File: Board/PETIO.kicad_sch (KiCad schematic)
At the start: 59 parts, among them CN2 PORT_CASSETTE_EDGE, CN3 PORT_IEEE_EDGE, IC11 74138N, IC12 74145N, IC15 VIA, IC17 PIA, IC20 PIA, IC21 7417N, IC22 7400N, IC23 7486N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

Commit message: preview for r1.3
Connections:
- net SCA renamed SDA
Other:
- note added: "1.0B: - fix IEEE488 pull up/down resistor values (again) 1.1A: - fully decode PIA addresses - replace some discrete Rs with RN7 - fix 2N2222 footprint for new BOM part 1.2A: - fix addressing 2nd SID by moving BA7 to IC9 - replace JP8 with a solder jumper (I/O block address) - replace 1N4148 with 1N4448 for lower fwd voltage drop 1.3A: - replace std PET kbd connector with extended / IDC conn"
- note added: "CBM-ULTIPET-V1.3A"
- note added: "CBM-ULTIPET-V1.3A-20250806"
- note removed: "1.0B: - fix IEEE488 pull up/down resistor values (again) 1.1A: - fully decode PIA addresses - replace some discrete Rs with RN7 - fix 2N2222 footprint for new BOM part 1.2A: - fix addressing 2nd SID by moving BA7 to IC9 - replace JP8 with a solder jumper (I/O block address) - replace 1N4148 with 1N4448 for lower fwd voltage drop"
- note removed: "CBM-ULTIPET-V1.2A"
- note removed: "CBM-ULTIPET-V1.2A-20241013"
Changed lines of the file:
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@@
 		)
 	)
-	(text "1.0B: \n- fix IEEE488 pull up/down resistor values (again)\n1.1A:\n- fully decode PIA addresses\n- replace some discrete Rs with RN7\n- fix 2N2222 footprint for new BOM part\n1.2A:\n- fix addressing 2nd SID by moving BA7 to IC9\n- replace JP8 with a solder jumper (I/O block address)\n- replace 1N4148 with 1N4448 for lower fwd voltage drop"
+	(text "1.0B: \n- fix IEEE488 pull up/down resistor values (again)\n1.1A:\n- fully decode PIA addresses\n- replace some discrete Rs with RN7\n- fix 2N2222 footprint for new BOM part\n1.2A:\n- fix addressing 2nd SID by moving BA7 to IC9\n- replace JP8 with a solder jumper (I/O block address)\n- replace 1N4148 with 1N4448 for lower fwd voltage drop\n1.3A:\n- replace std PET kbd connector with extended / IDC conn"
 		(exclude_from_sim no)
-		(at 314.706 351.536 0)
+		(at 278.638 347.472 0)
 		(effects
 			(font
@@
 		)
 	)
-	(text "CBM-ULTIPET-V1.2A"
+	(text "CBM-ULTIPET-V1.3A"
 		(exclude_from_sim no)
 		(at 464.82 340.36 0)
@@
 		)
 	)
-	(text "CBM-ULTIPET-V1.2A-20241013\n"
+	(text "CBM-ULTIPET-V1.3A-20250806\n"
 		(exclude_from_sim no)
 		(at 464.82 363.22 0)
@@
 		)
 	)
-	(global_label "SCA"
+	(global_label "SDA"
 		(shape input)
 		(at 76.2 275.59 180)

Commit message: more layout work on r1.3
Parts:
- IC15, IC17, IC20: footprint Package_DIP:DIP-42_W15.24mm_Socket_LongPads -> Package_DIP:DIP-40_W15.24mm_Socket_LongPads
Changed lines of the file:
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@@
 			)
 		)
-		(property "Footprint" "Package_DIP:DIP-42_W15.24mm_Socket_LongPads"
+		(property "Footprint" "Package_DIP:DIP-40_W15.24mm_Socket_LongPads"
 			(at 292.1 203.2 0)
 			(effects
@@
 			)
 		)
-		(property "Footprint" "Package_DIP:DIP-42_W15.24mm_Socket_LongPads"
+		(property "Footprint" "Package_DIP:DIP-40_W15.24mm_Socket_LongPads"
 			(at 154.94 132.08 0)
 			(effects
@@
 			)
 		)
-		(property "Footprint" "Package_DIP:DIP-42_W15.24mm_Socket_LongPads"
+		(property "Footprint" "Package_DIP:DIP-40_W15.24mm_Socket_LongPads"
 			(at 485.14 312.42 0)
 			(effects
@@
 			)
 		)
-		(property "Footprint" "Package_DIP:DIP-42_W15.24mm_Socket_LongPads"
+		(property "Footprint" "Package_DIP:DIP-40_W15.24mm_Socket_LongPads"
 			(at 497.84 312.42 0)
 			(effects
@@
 			)
 		)
-		(property "Footprint" "Package_DIP:DIP-42_W15.24mm_Socket_LongPads"
+		(property "Footprint" "Package_DIP:DIP-40_W15.24mm_Socket_LongPads"
 			(at 469.9 312.42 0)
 			(effects
@@
 			)
 		)
-		(property "Footprint" "Package_DIP:DIP-42_W15.24mm_Socket_LongPads"
+		(property "Footprint" "Package_DIP:DIP-40_W15.24mm_Socket_LongPads"
 			(at 287.02 116.84 0)
 			(effects

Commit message: add some jumper options, layout work
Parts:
- added JP18, JP22: JP1E, cbm_ultipet_v1:JP1, symbol cbm_ultipet_v1-eagle-import:JP1E
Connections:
- net DEC0: now also JP18.1
- net DEC1: now also JP22.1
- new net /IRQ: JP18.2
- new net /NMI: JP22.2
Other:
- note added: "1.0B: - fix IEEE488 pull up/down resistor values (again) 1.1A: - fully decode PIA addresses - replace some discrete Rs with RN7 - fix 2N2222 footprint for new BOM part 1.2A: - fix addressing 2nd SID by moving BA7 to IC9 - replace JP8 with a solder jumper (I/O block address) - replace 1N4148 with 1N4448 for lower fwd voltage drop 1.3A: - replace std PET kbd connector with extended / IDC conn - add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"
- note added: "CBM-ULTIPET-V1.3A-20250809"
- note added: "For use with two-row IDC keyboard connector"
- note removed: "1.0B: - fix IEEE488 pull up/down resistor values (again) 1.1A: - fully decode PIA addresses - replace some discrete Rs with RN7 - fix 2N2222 footprint for new BOM part 1.2A: - fix addressing 2nd SID by moving BA7 to IC9 - replace JP8 with a solder jumper (I/O block address) - replace 1N4148 with 1N4448 for lower fwd voltage drop 1.3A: - replace std PET kbd connector with extended / IDC conn"
- note removed: "CBM-ULTIPET-V1.3A-20250806"

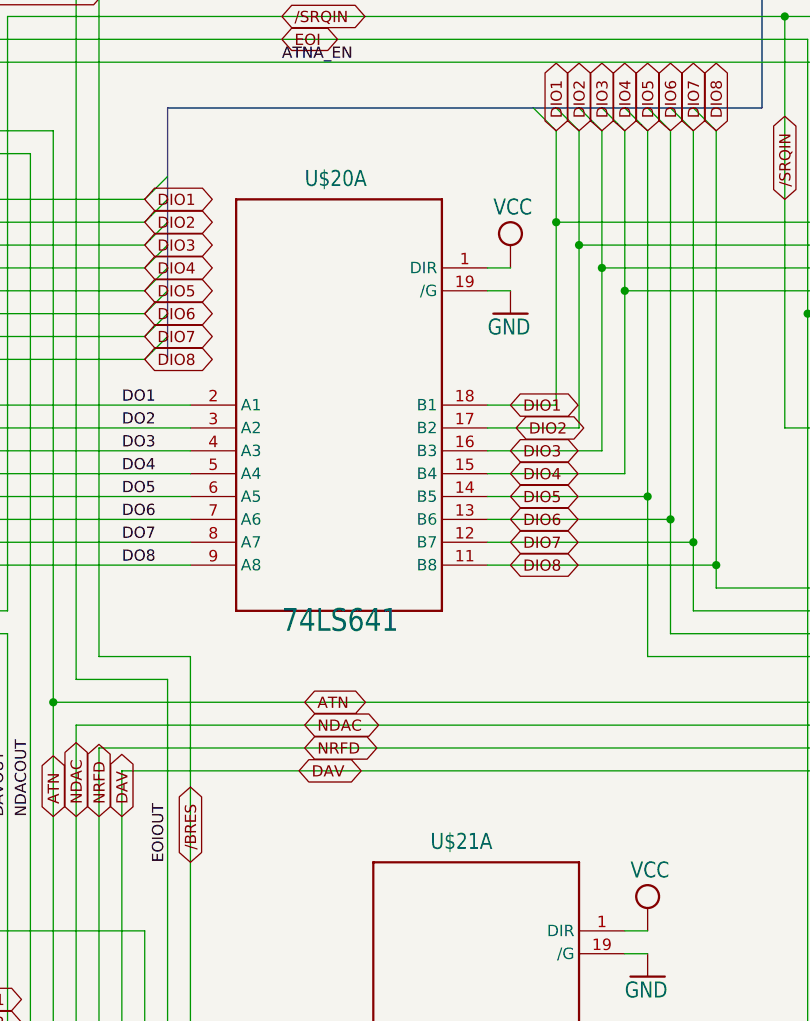
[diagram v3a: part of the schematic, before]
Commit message: rename U refs to UX*
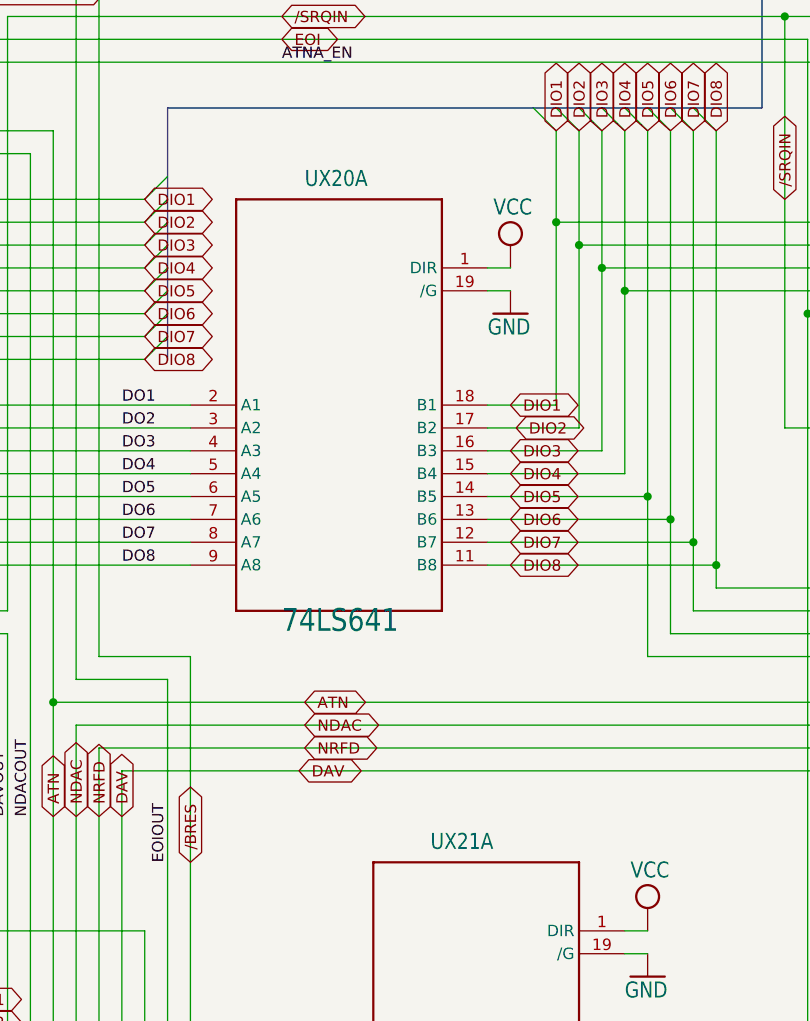
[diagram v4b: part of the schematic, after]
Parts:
- renumbered U$20 to UX20, U$21 to UX21
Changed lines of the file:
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@@
 		(on_board yes)
 		(dnp no)
-		(property "Reference" "U$20"
+		(property "Reference" "UX20"
 			(at 358.14 97.79 0)
 			(effects
@@
 			(project "cbm_ultipet_v1"
 				(path "/4dd2dd78-173f-4b46-8cce-4ed940435c94/6387d1ea-0693-42a3-ac70-75277d2d502e"
-					(reference "U$20")
+					(reference "UX20")
 					(unit 1)
 				)
@@
 		(on_board yes)
 		(dnp no)
-		(property "Reference" "U$21"
+		(property "Reference" "UX21"
 			(at 525.145 244.475 0)
 			(effects
@@
 			(project "cbm_ultipet_v1"
 				(path "/4dd2dd78-173f-4b46-8cce-4ed940435c94/6387d1ea-0693-42a3-ac70-75277d2d502e"
-					(reference "U$21")
+					(reference "UX21")
 					(unit 2)
 				)
@@
 		(on_board yes)
 		(dnp no)
-		(property "Reference" "U$21"
+		(property "Reference" "UX21"
 			(at 372.11 171.45 0)
 			(effects
@@
 			(project "cbm_ultipet_v1"
 				(path "/4dd2dd78-173f-4b46-8cce-4ed940435c94/6387d1ea-0693-42a3-ac70-75277d2d502e"
-					(reference "U$21")
+					(reference "UX21")
 					(unit 1)
 				)
@@
 		(on_board yes)
 		(dnp no)
-		(property "Reference" "U$20"
+		(property "Reference" "UX20"
 			(at 514.985 244.475 0)
 			(effects
@@
 			(project "cbm_ultipet_v1"
 				(path "/4dd2dd78-173f-4b46-8cce-4ed940435c94/6387d1ea-0693-42a3-ac70-75277d2d502e"
-					(reference "U$20")
+					(reference "UX20")
 					(unit 2)
 				)

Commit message: some layout fixes, more parts
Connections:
- net /NMI renamed /RES
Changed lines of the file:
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@@
 		)
 	)
-	(global_label "{slash}NMI"
-		(shape input)
-		(at 93.98 342.9 0)
-		(fields_autoplaced yes)
-		(effects
-			(font
-				(size 1.27 1.27)
-			)
-			(justify left)
-		)
-		(property "Intersheetrefs" "${INTERSHEET_REFS}"
-			(at 101.6824 342.9 0)
-			(effects
-				(font
-					(size 1.27 1.27)
-				)
-				(justify left)
-				(hide yes)
-			)
-		)
-	)
 	(global_label "BD7"
 		(shape bidirectional)
@@
 			(effects
 				(font
+					(size 1.27 1.27)
+				)
+				(justify left)
+				(hide yes)
+			)
+		)
+	)
+	(global_label "{slash}RES"
+		(shape input)
+		(at 93.98 342.9 0)
+		(fields_autoplaced yes)
+		(effects
+			(font
+				(size 1.27 1.27)
+			)
+			(justify left)
+		)
+		(property "Intersheetrefs" "${INTERSHEET_REFS}"
+			(at 101.9242 342.9 0)
+			(effects
+				(font

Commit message: add C64 restore
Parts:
- removed J14: Extended_PET_keyboard_connector, cbm_ultipet_v1:PET_Extended_Keyboard_Connector, symbol petkn:Extended_PET_keyboard_connector
- removed JP18, JP22: JP1E, cbm_ultipet_v1:JP1, symbol cbm_ultipet_v1-eagle-import:JP1E
- added C171: 51pF, cbm_ultipet_v1:C025-024X044, symbol cbm_ultipet_v1-eagle-import:C-EU025-024X044
- added C172: 360p, cbm_ultipet_v1:C025-024X044, symbol cbm_ultipet_v1-eagle-import:C-EU025-024X044
- added J2: New_PET_keyboard_connector, Connector_IDC:IDC-Header_2x10_P2.54mm_Vertical, symbol petkn:New_PET_keyboard_connector
- added P8: ~, cbm_ultipet_v1:C64KEYB, symbol cbm_ultipet_v1-eagle-import:PETKEYBD
- added Q4: BC557, cbm_ultipet_v1:TO92, symbol cbm_ultipet_v1-eagle-import:BC557
- added R68, R69: 1M, cbm_ultipet_v1:0207_2V, symbol cbm_ultipet_v1-eagle-import:R-EU_0207/2V
- added R70: 47k, cbm_ultipet_v1:0207_2V, symbol cbm_ultipet_v1-eagle-import:R-EU_0207/2V
- added R71: 100k, cbm_ultipet_v1:0207_7, symbol cbm_ultipet_v1-eagle-import:R-EU_0207/7
- added R72: 22, cbm_ultipet_v1:0207_2V, symbol cbm_ultipet_v1-eagle-import:R-EU_0207/2V
- added R82: 33, cbm_ultipet_v1:0207_2V, symbol cbm_ultipet_v1-eagle-import:R-EU_0207/2V
- added U14: NE555D, Package_SO:SOIC-8_3.9x4.9mm_P1.27mm, symbol Timer:NE555D
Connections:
- net DEC0: now also P8.12 (DEC0)
- net DEC1: now also P8.11 (DEC1)
- net DEC2: now also P8.10 (DEC2)
- net DEC3: now also P8.9 (DEC3)
- net DEC4: now also P8.8 (DEC4)
- net DEC5: now also P8.7 (DEC5)
- net DEC6: now also P8.6 (DEC6)
- net DEC7: now also P8.5 (DEC7)
- net DEC8: now also P8.4 (DEC8)
- net DEC9: now also P8.3 (DEC9)
- net GND: now also C172.1, J2.19 (GND), P8.1 (GND), Q4.3 (C), U14.1 (GND)
- net KI0: now also J2.20 (C1), P8.20 (KIN0)
- net KI1: now also J2.18 (C2), P8.19 (KIN1)
- net KI2: now also J2.16 (C3), P8.18 (KIN2)
- net KI3: now also J2.14 (C4), P8.17 (KIN3)
- net KI4: now also J2.12 (C5), P8.16 (KIN4)
- net KI5: now also J2.10 (C6), P8.15 (KIN5)
- net KI6: now also J2.8 (C7), P8.14 (KIN6)
- net KI7: now also J2.6 (C8), P8.13 (KIN7)
- net KSEL0: now also J2.17 (S0)
- net KSEL1: now also J2.15 (S1)
- net KSEL2: now also J2.13 (S2)
- net KSEL3: now also J2.11 (S3)
- net SCL: now also J2.5 (SCL)
- net SDA: now also J2.3 (SCA)
- net V33: now also J2.7 (VCC33)
- net VCC: now also J2.9 (VCC5), R68.1, R69.1, R70.2, U14.4 (R), U14.8 (VCC)
- net /IRQ: now also J2.2 (/IRQ)
- net /RES: now also J2.4 (/RES)
- net at P2.3 (RSTR): now also R68.2, R72.1
- new net: C172.2, R70.1, U14.6 (THR), U14.7 (DIS)
- new net: J2.1 (RESTORE), R72.2, R82.1
- new net: C171.1, R82.2
- new net: C171.2, R69.2, U14.2 (TR)
- new net: Q4.2 (B), R71.1
- new net: R71.2, U14.3 (Q)
- new net /NMI: Q4.1 (E)
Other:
- note added: "CBM-ULTIPET-V1.4A-20260507"
- note added: "RESTORE to NMI from C64"
- note removed: "CBM-ULTIPET-V1.3A-20250809"
- note removed: "For use with two-row IDC keyboard connector"
